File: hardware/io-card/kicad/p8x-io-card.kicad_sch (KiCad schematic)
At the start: 0 parts

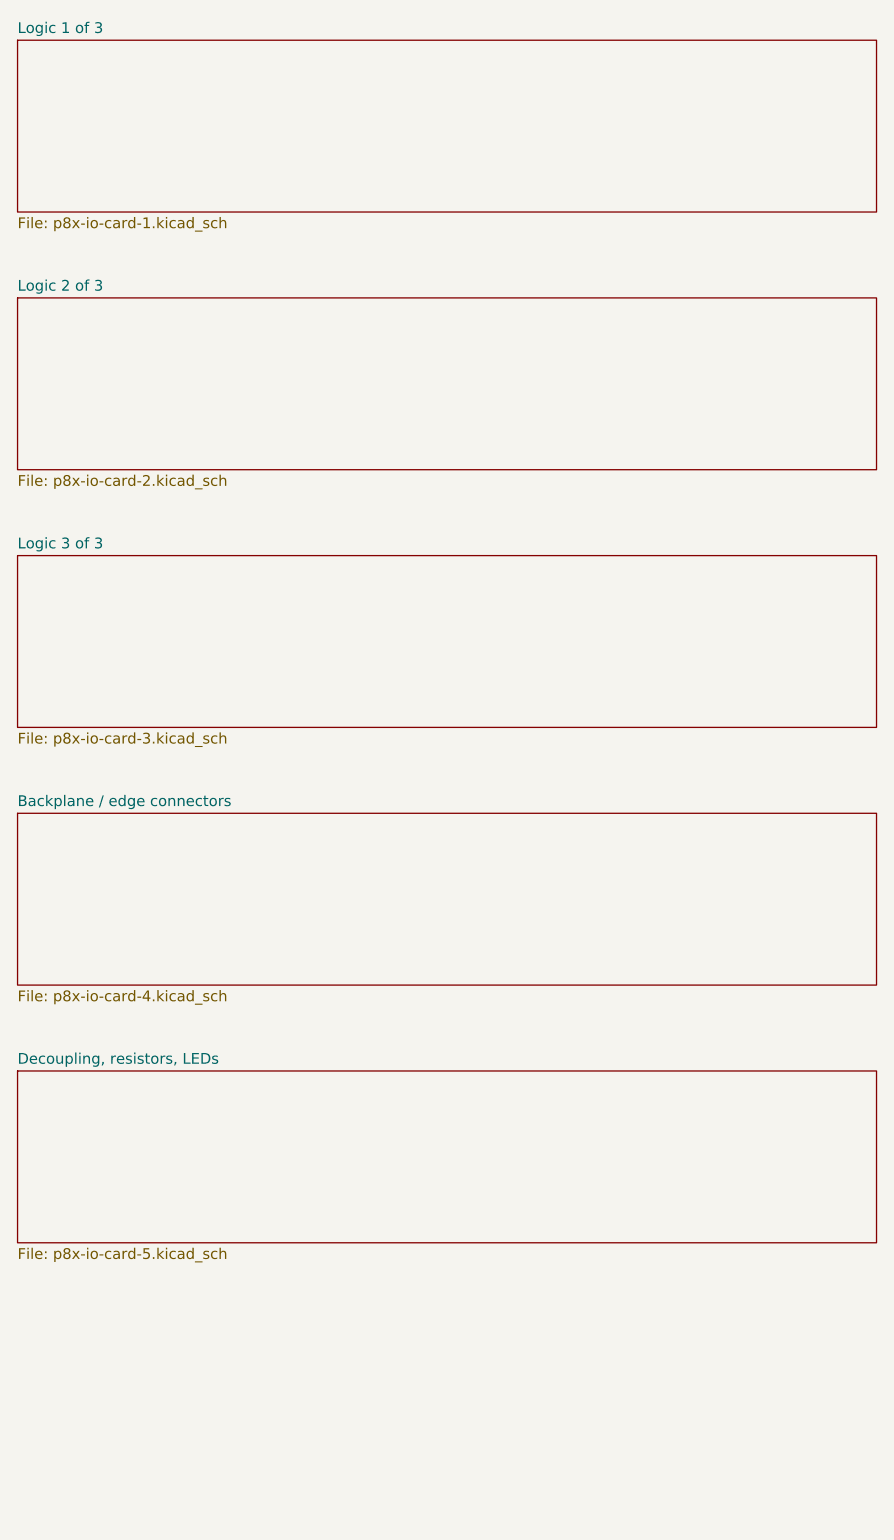
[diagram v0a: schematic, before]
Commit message: feat(sch): draw the io-card schematic by function
Group the io-card into functional sheets (address decode, switch/LED
ports, serial, bus monitor, RTC) with each block's resistors, LEDs,
crystals and connectors on the same sheet, so local nets are drawn as
wires: 18 -> ~330 wires. Orient wires by drawing side on this card
(FLOW_BY_SIDE) so the ACIA -> MAX232 round trip lays out left to right;
put the 6850 and MAX232 bus/TTL pins left and serial/RS-232 pins right;
draw the RX/TX swap jumpers with a schematic-only JMP2X3SWAP variant.
Netlist still matches the board (155 nets, 562 pins), ERC 0 errors.

Co-Authored-By: Claude Opus 5.5 <noreply@anthropic.com>
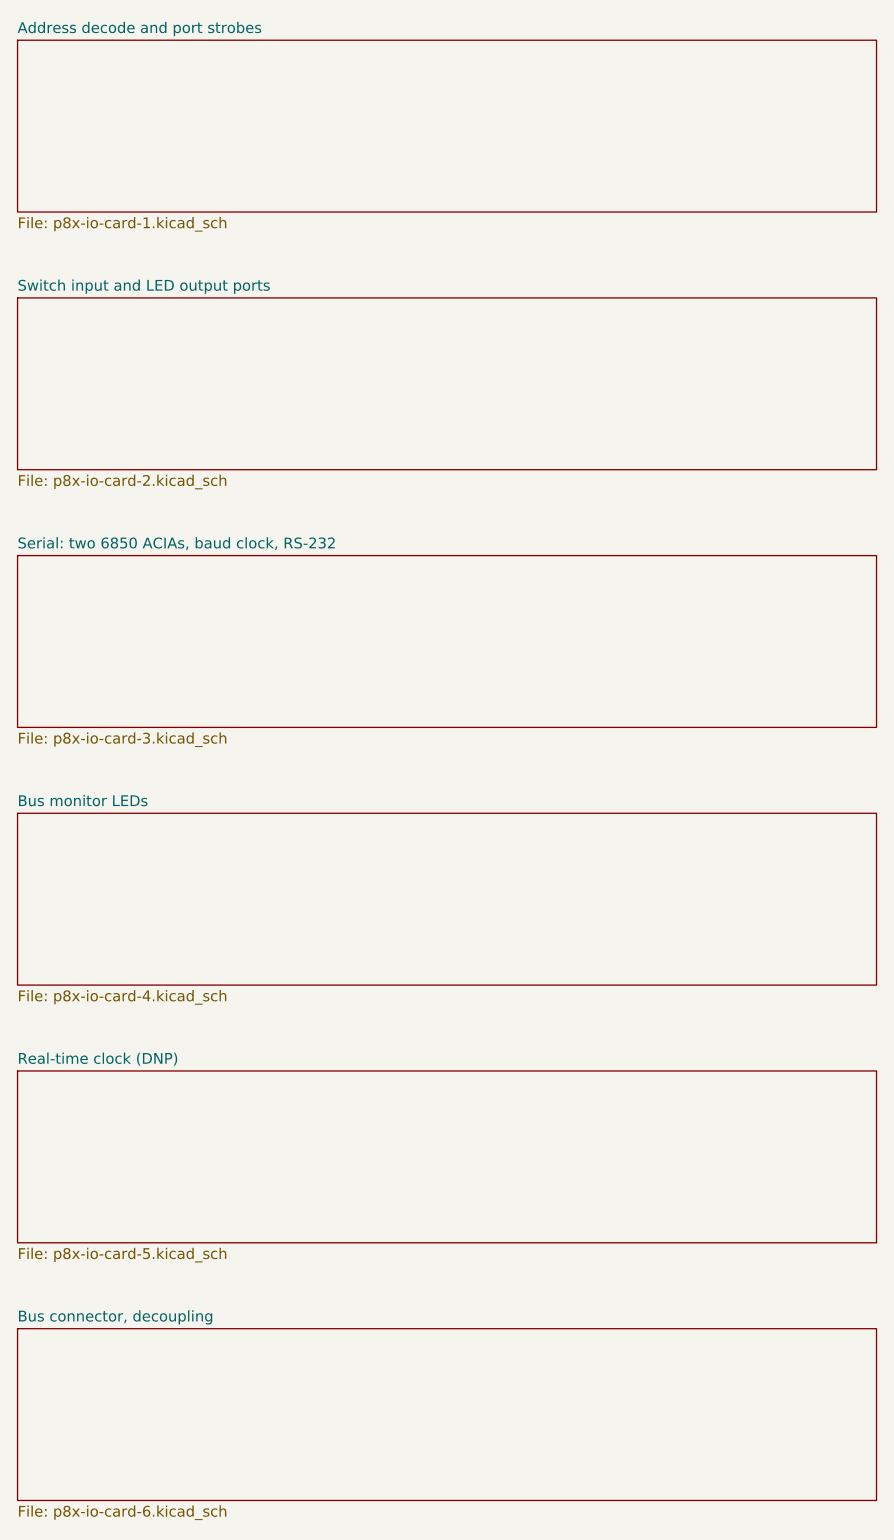
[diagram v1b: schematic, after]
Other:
- sheet Backplane / edge connectors renamed Bus monitor LEDs
- sheet Decoupling, resistors, LEDs renamed Real-time clock (DNP)
- sheet Logic 1 of 3 renamed Address decode and port strobes
- sheet Logic 2 of 3 renamed Switch input and LED output ports
- sheet Logic 3 of 3 renamed Serial: two 6850 ACIAs, baud clock, RS-232
- added sheet Bus connector, decoupling (p8x-io-card-6.kicad_sch)
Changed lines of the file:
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@@
   (sheet (at 25.40 30.48) (size 101.6 20.32) (fields_autoplaced yes)
     (stroke (width 0.1524) (type solid)) (fill (color 0 0 0 0.0000))
-    (property "Sheetname" "Logic 1 of 3" (at 25.40 29.78 0) (effects (font (size 1.27 1.27)) (justify left bottom)))
+    (property "Sheetname" "Address decode and port strobes" (at 25.40 29.78 0) (effects (font (size 1.27 1.27)) (justify left bottom)))
     (property "Sheetfile" "p8x-io-card-1.kicad_sch" (at 25.40 51.38 0) (effects (font (size 1.27 1.27)) (justify left top)))
     (instances (project "p8x-io-card" (path "/ed807a3d-9122-5982-9811-120926e12b80" (page "2"))))
@@
   (sheet (at 25.40 60.96) (size 101.6 20.32) (fields_autoplaced yes)
     (stroke (width 0.1524) (type solid)) (fill (color 0 0 0 0.0000))
-    (property "Sheetname" "Logic 2 of 3" (at 25.40 60.26 0) (effects (font (size 1.27 1.27)) (justify left bottom)))
+    (property "Sheetname" "Switch input and LED output ports" (at 25.40 60.26 0) (effects (font (size 1.27 1.27)) (justify left bottom)))
     (property "Sheetfile" "p8x-io-card-2.kicad_sch" (at 25.40 81.86 0) (effects (font (size 1.27 1.27)) (justify left top)))
     (instances (project "p8x-io-card" (path "/ed807a3d-9122-5982-9811-120926e12b80" (page "3"))))
@@
   (sheet (at 25.40 91.44) (size 101.6 20.32) (fields_autoplaced yes)
     (stroke (width 0.1524) (type solid)) (fill (color 0 0 0 0.0000))
-    (property "Sheetname" "Logic 3 of 3" (at 25.40 90.74 0) (effects (font (size 1.27 1.27)) (justify left bottom)))
+    (property "Sheetname" "Serial: two 6850 ACIAs, baud clock, RS-232" (at 25.40 90.74 0) (effects (font (size 1.27 1.27)) (justify left bottom)))
     (property "Sheetfile" "p8x-io-card-3.kicad_sch" (at 25.40 112.34 0) (effects (font (size 1.27 1.27)) (justify left top)))
     (instances (project "p8x-io-card" (path "/ed807a3d-9122-5982-9811-120926e12b80" (page "4"))))
@@
   (sheet (at 25.40 121.92) (size 101.6 20.32) (fields_autoplaced yes)
     (stroke (width 0.1524) (type solid)) (fill (color 0 0 0 0.0000))
-    (property "Sheetname" "Backplane / edge connectors" (at 25.40 121.22 0) (effects (font (size 1.27 1.27)) (justify left bottom)))
+    (property "Sheetname" "Bus monitor LEDs" (at 25.40 121.22 0) (effects (font (size 1.27 1.27)) (justify left bottom)))
     (property "Sheetfile" "p8x-io-card-4.kicad_sch" (at 25.40 142.82 0) (effects (font (size 1.27 1.27)) (justify left top)))
     (instances (project "p8x-io-card" (path "/ed807a3d-9122-5982-9811-120926e12b80" (page "5"))))
@@
   (sheet (at 25.40 152.40) (size 101.6 20.32) (fields_autoplaced yes)
     (stroke (width 0.1524) (type solid)) (fill (color 0 0 0 0.0000))
-    (property "Sheetname" "Decoupling, resistors, LEDs" (at 25.40 151.70 0) (effects (font (size 1.27 1.27)) (justify left bottom)))
+    (property "Sheetname" "Real-time clock (DNP)" (at 25.40 151.70 0) (effects (font (size 1.27 1.27)) (justify left bottom)))
     (property "Sheetfile" "p8x-io-card-5.kicad_sch" (at 25.40 173.30 0) (effects (font (size 1.27 1.27)) (justify left top)))
     (instances (project "p8x-io-card" (path "/ed807a3d-9122-5982-9811-120926e12b80" (page "6"))))
   )
+  (sheet (at 25.40 182.88) (size 101.6 20.32) (fields_autoplaced yes)
+    (stroke (width 0.1524) (type solid)) (fill (color 0 0 0 0.0000))
+    (property "Sheetname" "Bus connector, decoupling" (at 25.40 182.18 0) (effects (font (size 1.27 1.27)) (justify left bottom)))
+    (property "Sheetfile" "p8x-io-card-6.kicad_sch" (at 25.40 203.78 0) (effects (font (size 1.27 1.27)) (justify left top)))
+    (instances (project "p8x-io-card" (path "/ed807a3d-9122-5982-9811-120926e12b80" (page "7"))))
+  )
   (sheet_instances (path "/" (page "1")))
